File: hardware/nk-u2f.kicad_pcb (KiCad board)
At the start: 2 copper layers, 21.8 x 16.3 mm, 23 parts, among them J1 USB_Plug, P1 TouchPAD, U1 EFM8UB1xFxxG-QFN20, U2 MTCH101, U3 DF5A5.6JE, U4 ATECC508A

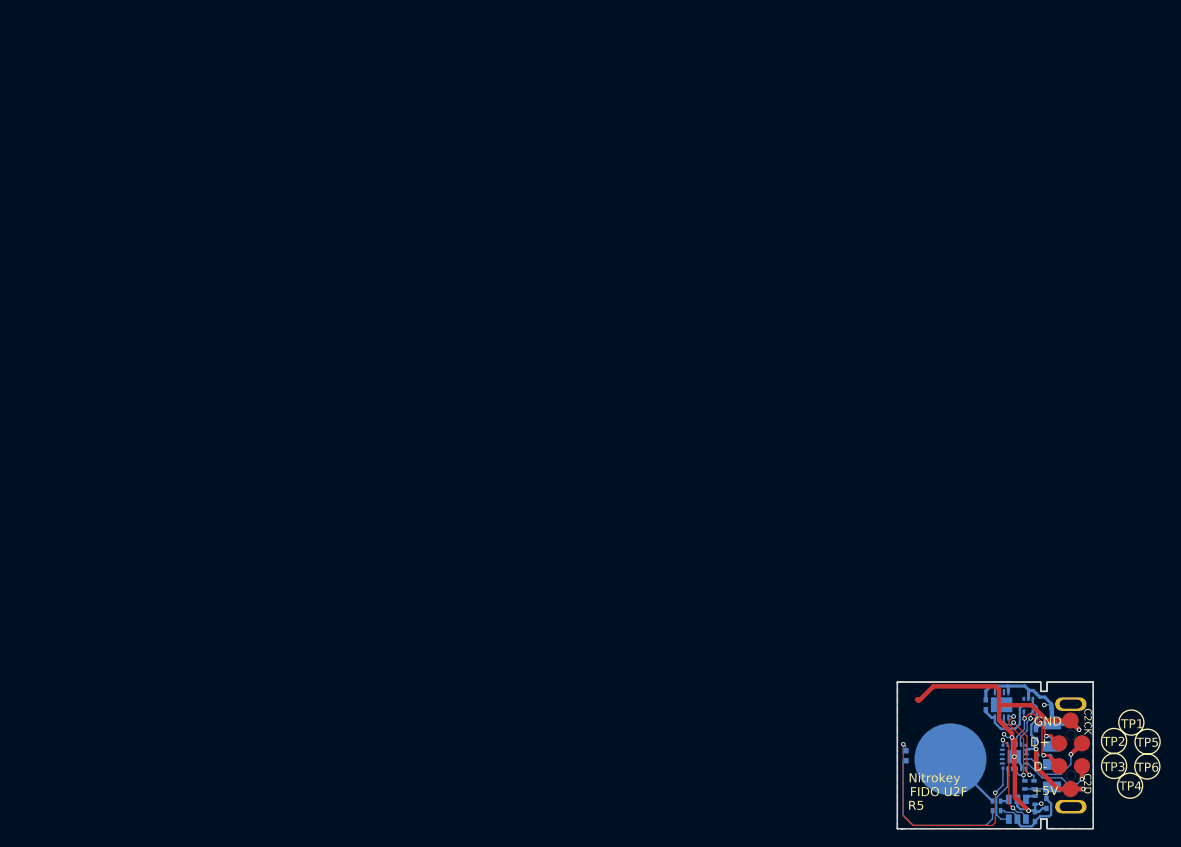
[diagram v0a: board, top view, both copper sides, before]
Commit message: REV6  - MTCH101 touch controller IC replaced with a simplier capacitive voltage divider solution.  - Board size shrunken to fit inside an USB A socket
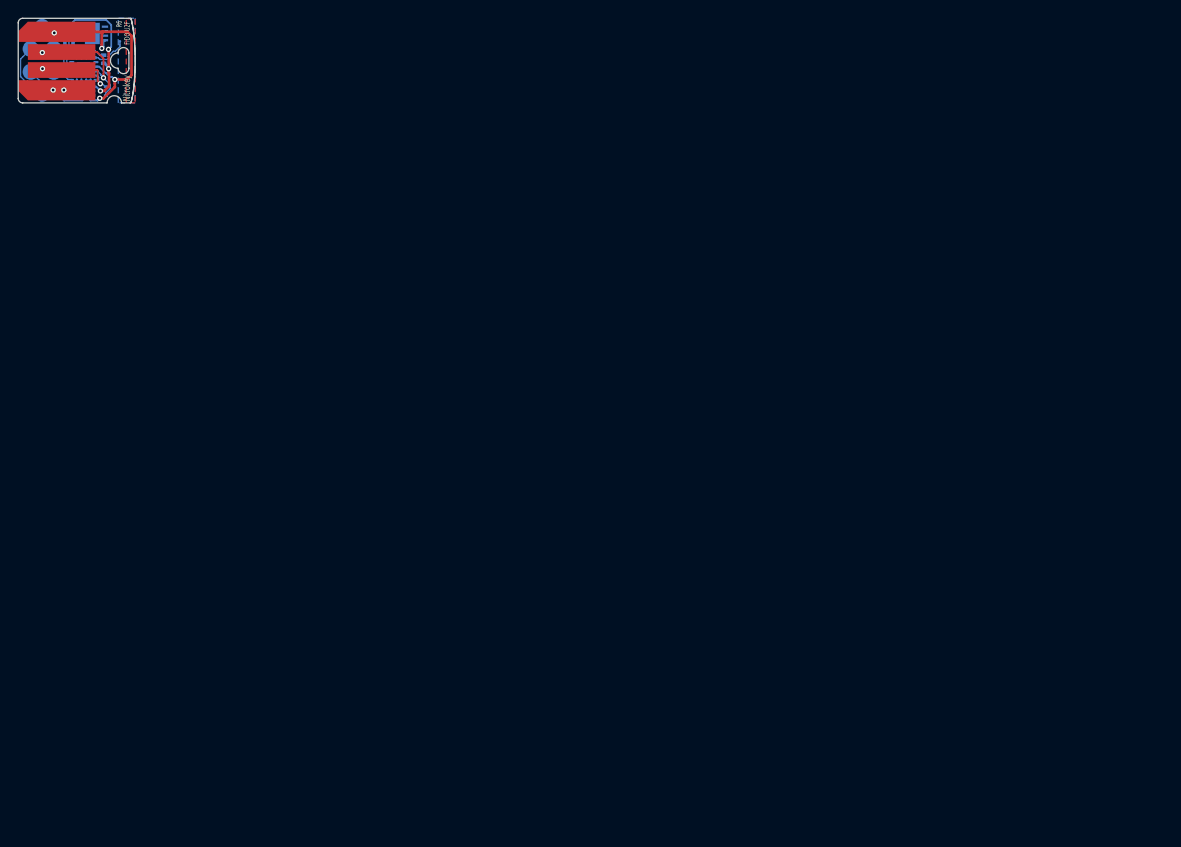
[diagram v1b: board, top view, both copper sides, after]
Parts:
- removed C2: 0.1uF, Capacitors_SMD:C_0402
- removed R1: 4K7, Resistors_SMD:R_0402
- removed R2: 10K, Resistors_SMD:R_0402
- removed TP1, TP2, TP3, TP4, TP5, TP6: debug-pin, footprints:Prog_Pad_Circular
- removed U2: MTCH101, TO_SOT_Packages_SMD:SOT-23-6
- added J2: prog_conn_nk, footprints:prog_conn_nk, B.Cu at (19.7, 21.8)
- J1: footprint footprints:USB-A-PLUG -> footprints:USB-PCB
- P1: footprint footprints:TouchPad -> TouchPad
- U1: value EFM8UB1xFxxG-QFN20 -> EFM8UB30F40G-A
- moved J1 144.6 mm to (16.9, 27.4)
- moved R7 135.8 mm to (22.7, 19.0), turned to 0 degrees
- moved C3 134.5 mm to (22.1, 25.7), turned to 180 degrees
- moved R5 134.5 mm to (22.7, 19.9), turned to 0 degrees
- moved R3 131.7 mm to (24.7, 20.6)
- moved R4 129.7 mm to (24.0, 24.9), turned to 180 degrees
- moved U1 128.6 mm to (24.3, 22.7), turned to 180 degrees
- moved C4 127.6 mm to (24.1, 25.7), turned to 0 degrees
- moved C1 126.9 mm to (22.4, 18.1), turned to 180 degrees
- moved U4 125.6 mm to (25.3, 18.8), turned to 180 degrees
- moved U3 123.7 mm to (26.1, 25.2), turned to 0 degrees
- moved P1 122.0 mm to (28.3, 19.7), turned to 0 degrees
- moved D1 118.0 mm to (26.5, 21.6)
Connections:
- D1 pad 1: /LED -> Net-(D1-Pad1)
- D1 pad 2: Net-(D1-Pad2) -> /+5V
- P1 pad 1: Net-(P1-Pad1) -> /Button
- R3 pad 1: Net-(D1-Pad2) -> /LED
- R3 pad 2: /+5V -> Net-(D1-Pad1)
- U1 pad 15: /Button_reset -> (no net)
- U1 pad 17: /RX -> (no net)
- U1 pad 18: /TX -> (no net)
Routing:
- net /GND: track 65.8 -> 41.3 mm, vias 7 -> 4
- net /LED: track 26.0 -> 1.77 mm, vias 2 -> 0
- net Net-(D1-Pad2): track 17.8 -> 0.00 mm
- net /+5V: track 44.7 -> 30.6 mm, vias 2 -> 5
- net /Button_reset: track 7.43 -> 0.00 mm
- net /Button: track 10.7 -> 4.16 mm, vias 2 -> 0
- net Net-(P1-Pad1): track 6.58 -> 0.00 mm
- net /SDA: track 10.0 -> 4.64 mm, vias 2 -> 0
- net /HD-: track 14.1 -> 8.97 mm
- net /SCL: track 10.4 -> 6.79 mm, vias 2 -> 0
- net /C2D: track 9.04 -> 5.94 mm, vias 1 -> 0
- net Net-(D1-Pad1): track 0.00 -> 1.58 mm
- net Net-(R2-Pad2): track 1.16 -> 0.00 mm
- net /C2CK: track 10.4 -> 11.4 mm, vias 1 -> 0
- net Net-(R1-Pad2): track 1.01 -> 0.00 mm
- added copper zone on B.Cu, net /Button
- removed copper zone on B.Cu, net /GND
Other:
- board size 21.8 x 16.3 mm -> 13 x 9.4 mm
- net class Default: clearance 0.15 -> 0.1524; trace_width 0.15 -> 0.1524; via_dia 0.5 -> 0.6
- net class GND removed
- net class VBUS removed
- net class VDD removed
- rule pad_to_mask_clearance: 0.05 -> 0.07
- rule trace_clearance: 0.15 -> 0.1524
- rule via_min_size: 0.5 -> 0.4
- board text added: "C2K"
- board text added: "R6"
- board text added: "UFQFPN32 - STM32F042x4 - STM32L442KC 24-QFN - Silicon Labs - EFM32HG308 - EFM32HG350 - NXP - MKL27Z32Vxx4"
- board text removed: "C2CK"
- board text removed: "R5"
